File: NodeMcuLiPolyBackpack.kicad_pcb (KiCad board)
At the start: 2 copper layers, 15.2 x 26.7 mm, 14 parts, among them P1 Switch, P2 G BAT, P3 Battery, P4 G 5V, U1 MCP73831

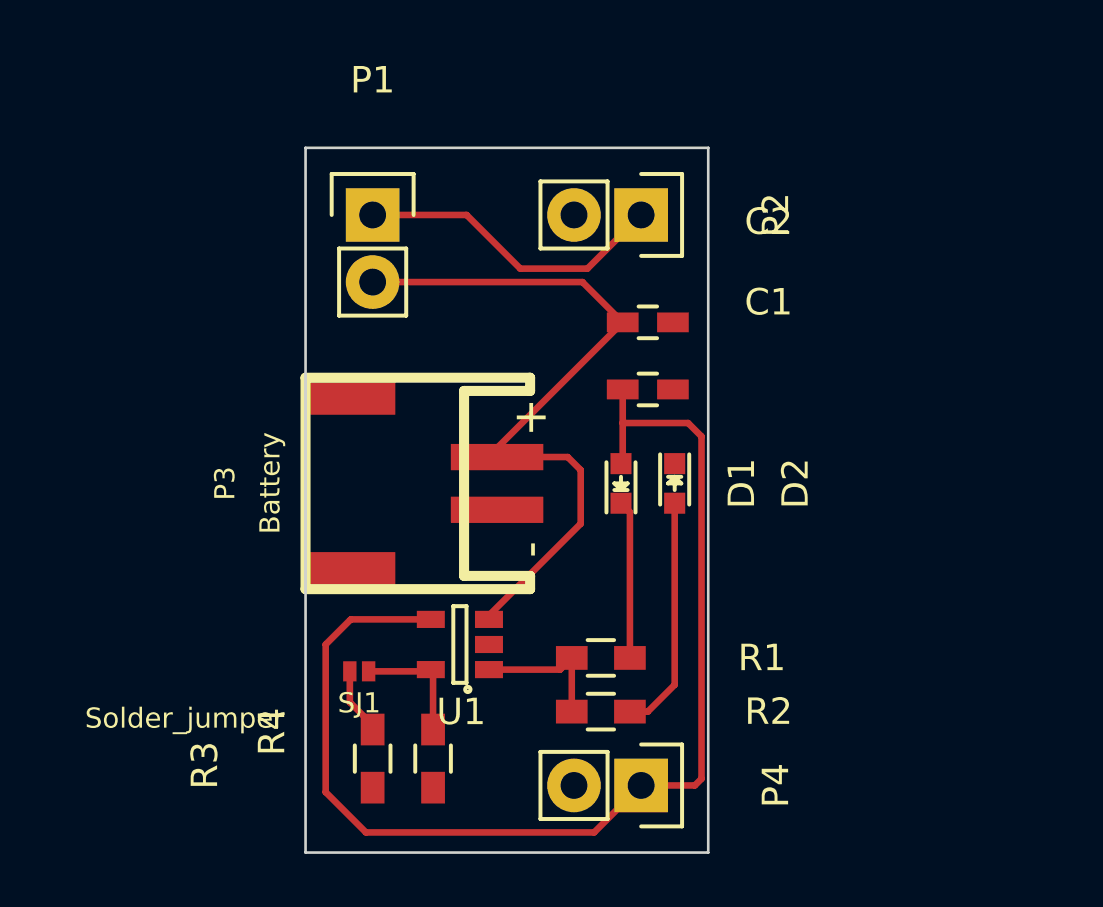
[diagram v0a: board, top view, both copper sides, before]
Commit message: Agregados medidas de orificios y pines.
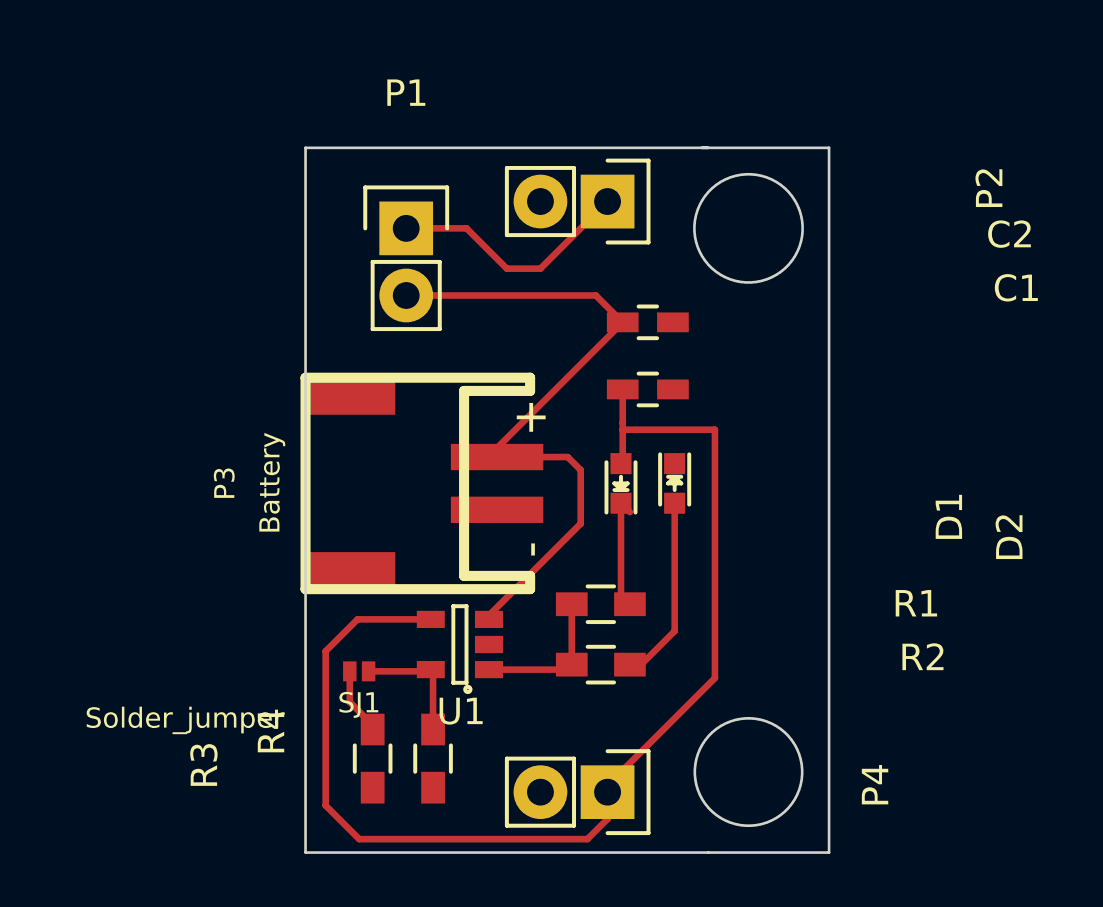
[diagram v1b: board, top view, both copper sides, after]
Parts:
- moved R1 2.03 mm to (138.2, 112.5)
- moved R2 1.78 mm to (138.2, 114.8)
- moved P1 1.37 mm to (130.8, 98.3)
- moved P2 1.37 mm to (138.4, 97.3)
- moved P4 1.30 mm to (138.4, 119.6)
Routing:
- net Net-(P1-Pad1): track 11.8 -> 9.30 mm
- net Net-(D2-Pad2): track 8.99 -> 7.06 mm
- net Net-(D1-Pad1): track 5.99 -> 4.44 mm
- net /VBat: track 27.6 -> 26.1 mm
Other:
- board size 15.2 x 26.7 mm -> 19.8 x 26.7 mm

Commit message: Logo, reacomodo  v1.0
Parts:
- moved C1 13.1 mm to (134.0, 116.1), turned to 270 degrees
- moved R2 8.41 mm to (139.6, 106.5)
- moved U1 5.22 mm to (138.0, 114.9)
- moved D1 5.21 mm to (144.0, 109.3), turned to 0 degrees
- moved SJ1 4.89 mm to (129.8, 119.9)
- moved R1 3.52 mm to (139.6, 109.3)
- moved D2 3.25 mm to (143.9, 106.5), turned to 180 degrees
- moved R4 2.25 mm to (129.2, 116.1), turned to 270 degrees
- moved R3 2.24 mm to (131.6, 116.1), turned to 270 degrees
- moved P4 1.42 mm to (139.8, 119.9)
- moved P2 1.40 mm to (139.8, 97.3)
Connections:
- P1 pad 1: Net-(P1-Pad1) -> /VBat
- P2 pad 1: Net-(P1-Pad1) -> /VBat
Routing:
- net /VBat: track 26.1 -> 43.8 mm
- net Net-(P1-Pad1): track 9.30 -> 0.00 mm
- net Net-(R1-Pad1): track 5.50 -> 11.8 mm
- net Net-(R3-Pad2): track 4.68 -> 10.6 mm
- net Net-(D2-Pad2): track 7.06 -> 2.39 mm
- net Net-(D1-Pad1): track 4.44 -> 2.47 mm
- net /VBUS: track 44.5 -> 45.7 mm
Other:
- outline, holes or cut-outs redrawn
- board text added: "100 mA Default Short jumper 0.5 A"

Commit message: Fix autosave
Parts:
- added LOGO: , mdo:LOGO, B.Cu at (128.8, 115.8)
